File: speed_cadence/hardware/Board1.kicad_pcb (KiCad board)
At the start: 2 copper layers, 32.8 x 58.2 mm, 17 parts, among them IC1 AH1912-W-7, J1 DX07S016JA3R1500, J2 Conn_01x04_Pin, J3 Conn_ST_STDC14, SW1 SW_Push, U1 STM32F042G6U6TR, U2 TS2940CW33_RPG, U4 TJA1051T-3

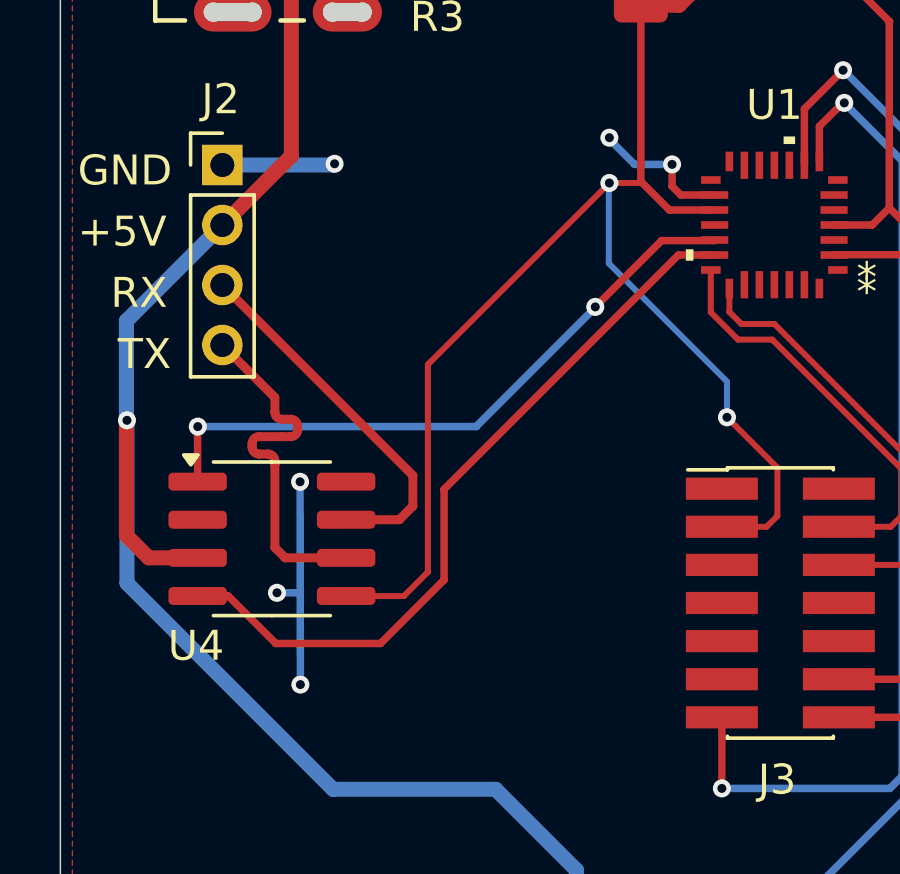
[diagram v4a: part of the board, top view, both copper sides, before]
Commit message: Updated differential pair routing
CANH is now CAN+
CANL is now CAN- for KiCAD to recognize the differential pair.
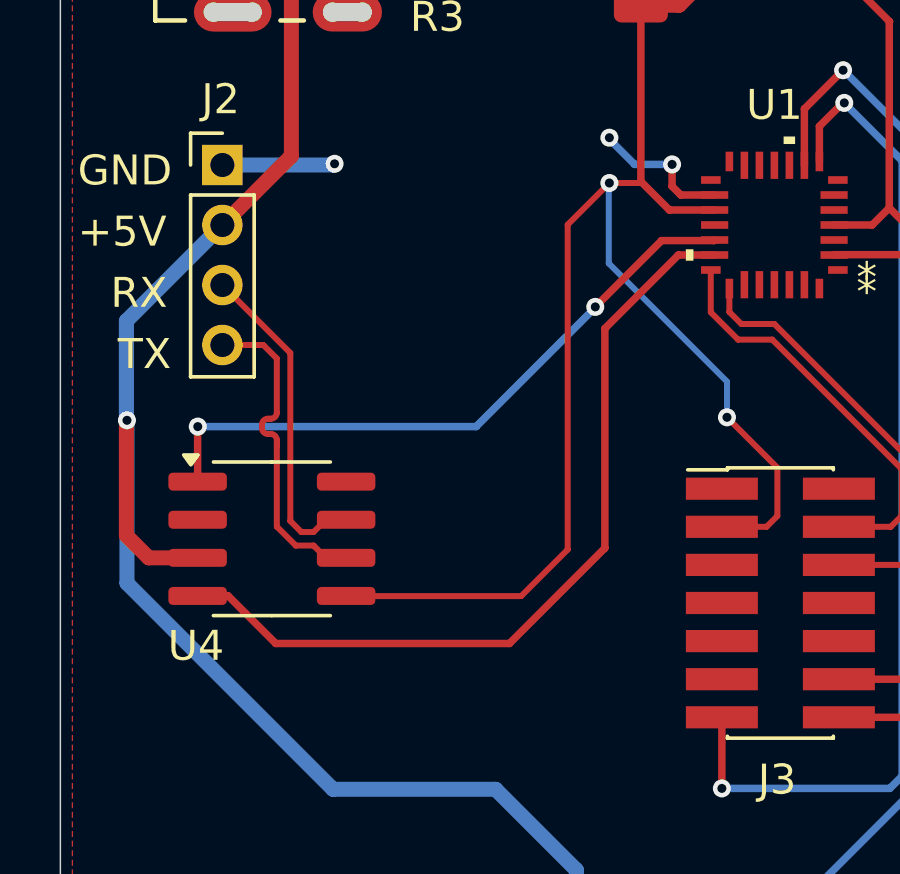
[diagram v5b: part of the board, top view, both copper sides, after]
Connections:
- net CAN_H renamed CAN+
- net CAN_L renamed CAN-
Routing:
- net GND: track 26.4 -> 18.8 mm, vias 7 -> 4
- net CAN_RX: track 25.0 -> 27.5 mm
- net +3V3: track 47.6 -> 49.9 mm
- net CAN+: track 12.4 -> 11.0 mm
- net CAN-: track 12.4 -> 11.0 mm
